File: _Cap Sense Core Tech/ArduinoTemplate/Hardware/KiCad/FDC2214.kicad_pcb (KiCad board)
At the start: 2 copper layers, 24 parts, among them IC1 FDC2214QRGHRQ1, J1 Conn_01x07, J2 Conn_01x08, Y1 ECS-2033-400-BN

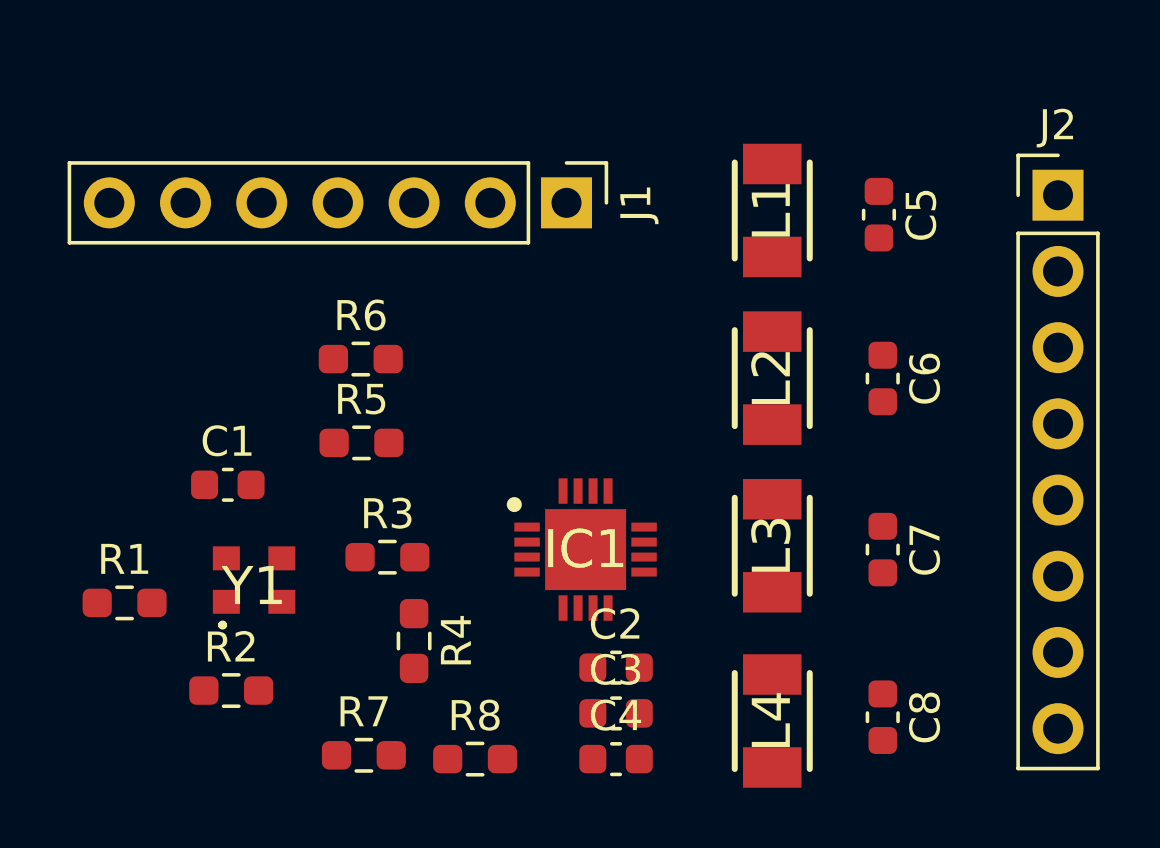
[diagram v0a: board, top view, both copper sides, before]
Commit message: modify layout
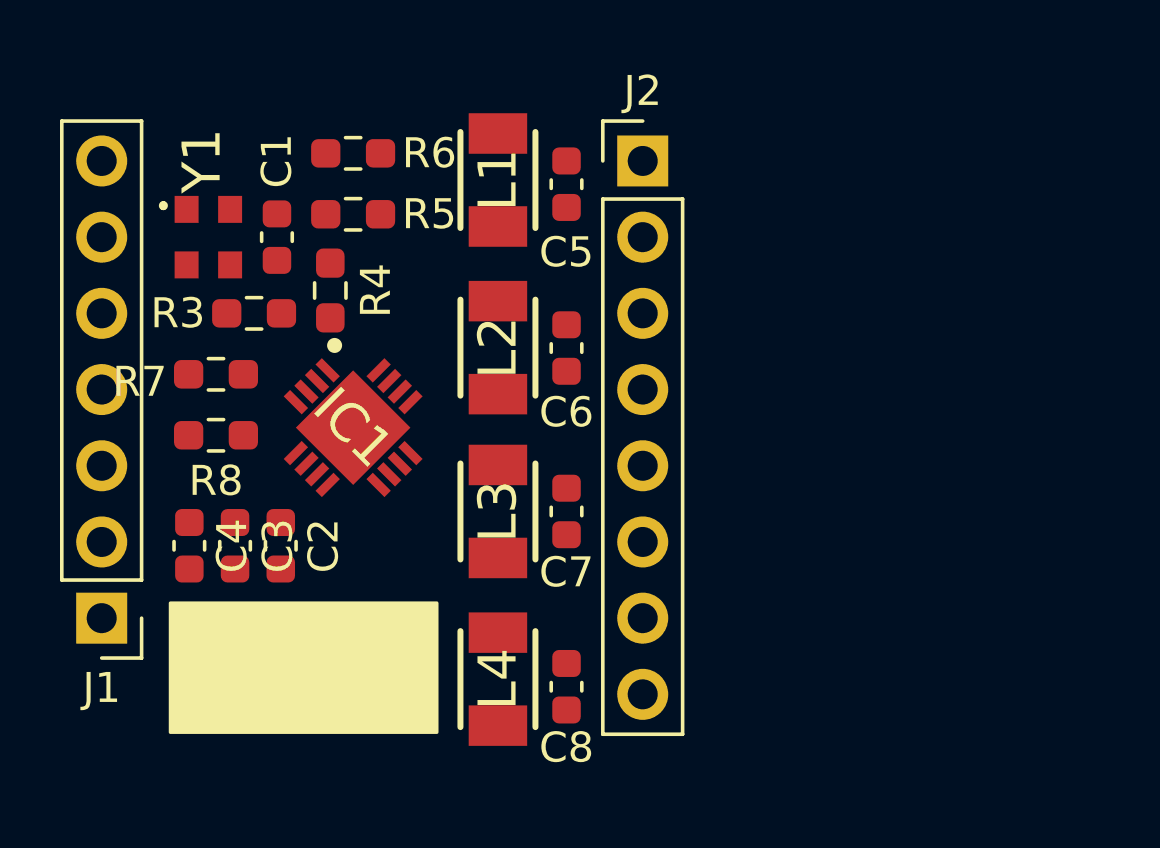
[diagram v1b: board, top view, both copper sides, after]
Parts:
- removed R1, R2: 0, Resistor_SMD:R_0603_1608Metric_Pad0.98x0.95mm_HandSolder
- moved J1 20.8 mm to (175.3, 144.8), turned to 180 degrees
- moved C4 15.9 mm to (178.2, 142.4), turned to 270 degrees
- moved J2 13.9 mm to (193.3, 129.5)
- moved C3 13.9 mm to (179.7, 142.4), turned to 270 degrees
- moved R8 13.8 mm to (179.1, 138.7), turned to 180 degrees
- moved R7 13.6 mm to (179.1, 136.7)
- moved R4 12.0 mm to (182.9, 133.9), turned to 90 degrees
- moved C2 11.9 mm to (181.2, 142.4), turned to 270 degrees
- moved Y1 11.5 mm to (178.8, 132.1), turned to 270 degrees
- moved C7 10.6 mm to (190.8, 141.2)
- moved C6 10.6 mm to (190.8, 135.8)
- moved C8 10.6 mm to (190.8, 147.1)
- moved C5 10.5 mm to (190.8, 130.3)
- moved R3 9.26 mm to (180.3, 134.6)
- moved L4 9.25 mm to (188.5, 146.8)
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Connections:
- IC1 pad 4: Addr -> ADDR
- J1 pad 2: +3V3 -> SD
- J1 pad 3: SD -> INTB
- J1 pad 4: INTB -> ADDR
- J1 pad 5: ADDR -> +3V3
- R7 pad 2: Addr -> ADDR
- R8 pad 1: Addr -> ADDR
